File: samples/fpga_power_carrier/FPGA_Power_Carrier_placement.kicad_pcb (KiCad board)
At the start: 2 copper layers, 50 x 40 mm, 4 parts, among them U1 AP62300, U2 AP62300, U3 AP62300, U4 TLV75518

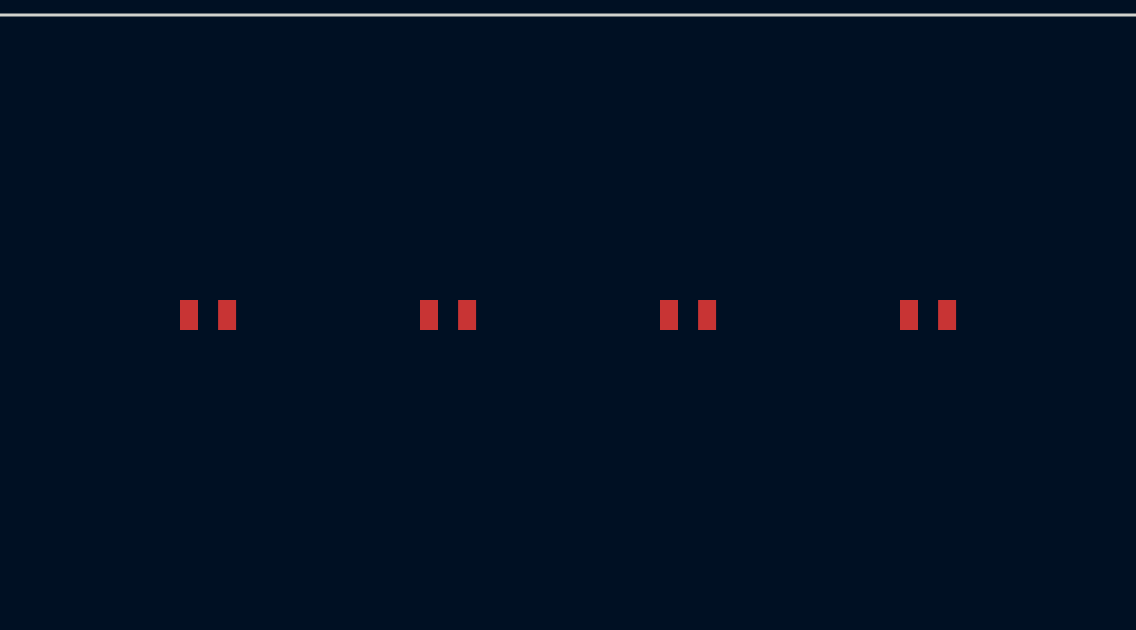
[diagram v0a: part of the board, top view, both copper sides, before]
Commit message: chore: regenerate 8 sample designs against v0.27.0 engine
All 8 samples pass full validation (0 ERC errors):
- led_power_indicator, iot_sensor_node, usb_regulated_supply,
  usb_uart_bridge, oled_display_module, battery_iot_sensor,
  motor_controller, fpga_power_carrier

New artifacts per sample: .kicad_sch, _test_points.csv, _pinout.csv,
canonical_spec.yaml, design_ir.json, validation_report.json; MCU samples
also emit sdkconfig.defaults / .ioc stubs.

Also adds samples/*/svg/ to .gitignore — schematic SVG exports are
regenerable and too large to track.

zigbee_humidistat deferred: non-deterministic schematic output across
two generation runs (text annotation ordering vs sheet_instances).
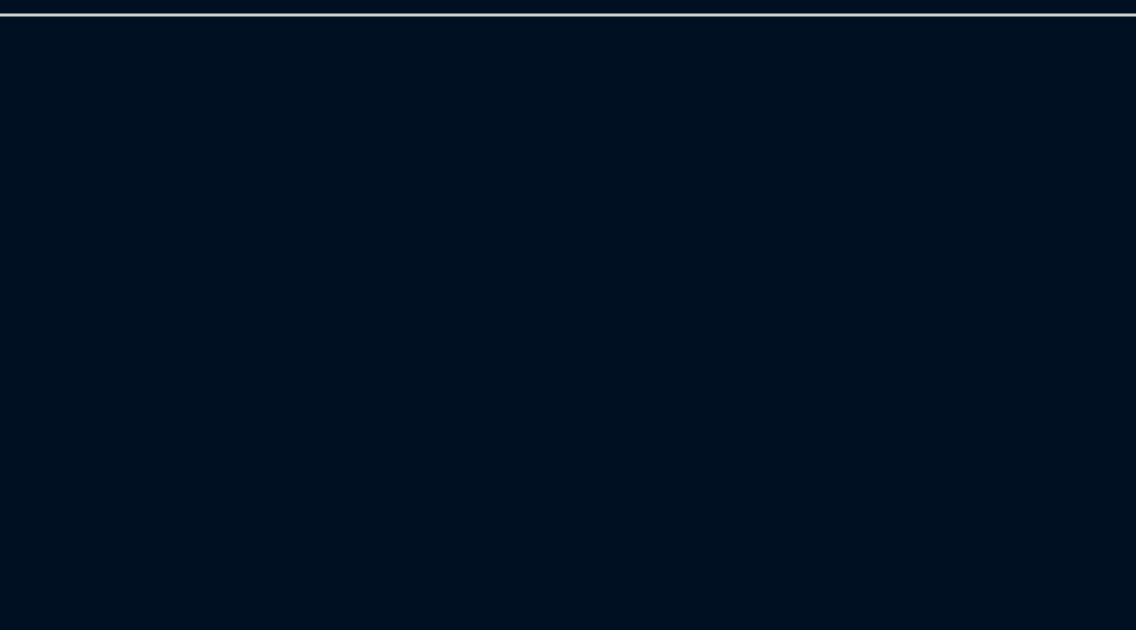
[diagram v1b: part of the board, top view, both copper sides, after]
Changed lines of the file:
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@@
-(kicad_pcb (version 20240108) (generator "schematic_engine")
+(kicad_pcb (version 20240108) (generator "schematic_engine placement_preview")
   (general (thickness 1.6) (legacy_teardrops no))
   (layers
@@
       (effects (font (size 1.0 1.0) (thickness 0.15)))
     )
-    (pad "1" smd rect (at 0.00 0) (size 0.6 1.0) (layers "F.Cu" "F.Paste" "F.Mask") (net 15 "VIN_12V"))
-    (pad "2" smd rect (at 1.27 0) (size 0.6 1.0) (layers "F.Cu" "F.Paste" "F.Mask") (net 7 "GND"))
   )
   (footprint "SOT-23-6"
@@
       (effects (font (size 1.0 1.0) (thickness 0.15)))
     )
-    (pad "1" smd rect (at 0.00 0) (size 0.6 1.0) (layers "F.Cu" "F.Paste" "F.Mask") (net 15 "VIN_12V"))
-    (pad "2" smd rect (at 1.27 0) (size 0.6 1.0) (layers "F.Cu" "F.Paste" "F.Mask") (net 7 "GND"))
   )
   (footprint "SOT-23-6"
@@
       (effects (font (size 1.0 1.0) (thickness 0.15)))
     )
-    (pad "1" smd rect (at 0.00 0) (size 0.6 1.0) (layers "F.Cu" "F.Paste" "F.Mask") (net 15 "VIN_12V"))
-    (pad "2" smd rect (at 1.27 0) (size 0.6 1.0) (layers "F.Cu" "F.Paste" "F.Mask") (net 7 "GND"))
   )
   (footprint "SOT-23-5"
@@
       (effects (font (size 1.0 1.0) (thickness 0.15)))
     )
-    (pad "1" smd rect (at 0.00 0) (size 0.6 1.0) (layers "F.Cu" "F.Paste" "F.Mask") (net 14 "VDD_3P3"))
-    (pad "2" smd rect (at 1.27 0) (size 0.6 1.0) (layers "F.Cu" "F.Paste" "F.Mask") (net 7 "GND"))
   )
   (gr_line (start 0.00 0.00) (end 50.00 0.00) (stroke (width 0.1) (type solid)) (layer "Edge.Cuts"))
